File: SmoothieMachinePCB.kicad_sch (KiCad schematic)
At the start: 50 parts, among them J1 Up Button, J10 Vin, J11 LCD I2C Adapter, J2 Down Button, J3 Next Ingredient Button, J4 Next Recipe Button, J5 Solenoid Valve, J6 Stepper Motor 2, J8 Stepper Motor 1, J9 LoadCell, U1 ESP32-S3-WROOM-2, U2 FSA2567MPX, U3 DRV8825PWP, U4 VN10KN3-G, U6 NAU7802SGI, U7 XL1509-3.3

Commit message: Integrated Microcontroller Essential Stuff into Schematic and Assigned Footprints
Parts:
- added C4: 1uF, Capacitor_SMD:C_0805_2012Metric_Pad1.18x1.45mm_HandSolder, symbol Device:C
- added J12: Conn_ARM_JTAG_SWD_10, Connector_IDC:IDC-Header_2x05_P2.54mm_Vertical, symbol Connector:Conn_ARM_JTAG_SWD_10
- added J7: Conn_01x05, Connector_Molex:Molex_KK-254_AE-6410-05A_1x05_P2.54mm_Vertical, symbol Connector_Generic:Conn_01x05
- added JP1: SolderJumper_3_Open, Jumper:SolderJumper-3_P2.0mm_Open_TrianglePad1.0x1.5mm, symbol Jumper:SolderJumper_3_Open
- added JP2, JP3: SolderJumper_2_Open, Jumper:SolderJumper-2_P1.3mm_Open_TrianglePad1.0x1.5mm, symbol Jumper:SolderJumper_2_Open
- added Q1, Q2: SS8050, Package_TO_SOT_SMD:SOT-23, symbol Transistor_BJT:SS8050
- added R15, R16, R17, R7: 10k, Resistor_SMD:R_0805_2012Metric_Pad1.20x1.40mm_HandSolder, symbol Device:R
- added R2, R4: 1k, Resistor_SMD:R_0805_2012Metric_Pad1.20x1.40mm_HandSolder, symbol Device:R
- added R6: 100k, Resistor_SMD:R_0805_2012Metric_Pad1.20x1.40mm_HandSolder, symbol Device:R
- added SW1, SW2: SW_Push, Button_Switch_SMD:SW_SPST_B3S-1000, symbol Switch:SW_Push
- C6: value 22uF -> 100nF
- C7: value 0.1uF -> 10uF
- R5: value 10k -> 100k
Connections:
- net GND: now also C5.2, C4.2, J12.3 (GND), J12.5 (GND), J12.9 (GNDDetect), J7.5 (Pin_5), JP1.3 (B), SW1.1, SW2.1; no longer C5.1
- net MODE0: now also U1.7 (IO7); no longer U1.15 (IO3)
- net NSLEEP: now also U1.6 (IO6); no longer U1.16 (IO46)
- net VDD33: now also JP1.1 (A), JP2.2 (B), JP3.2 (B), R2.2, R6.1; no longer C1.1, L1.2, U7.3 (FB)
- net GPIO0_STRAPPING: now reaches U1.27 (IO0)
- net GPIO0_STRAPPING: now also C5.1, R5.2, R15.2, SW2.2
- new net: Q2.1 (B), R17.2
- new net: Q2.3 (C), R15.1
- new net: C1.1, JP2.1 (A), L1.2, U7.3 (FB)
- new net: JP1.2 (C), R4.2
- new net: Q1.3 (C), R7.1
- new net: J12.1 (VTref), JP3.1 (A)
- new net: Q1.1 (B), R16.2
- new net CHIP_PU: C4.1, J12.10 (~{RESET}), R6.2, R7.2, SW1.2, U1.3 (EN)
- new net DTR: J7.2 (Pin_2), Q2.2 (E), R16.1
- new net GPIO3_STRAPPING: R4.1, U1.15 (IO3)
- new net GPIO46_STRAPPING: R2.1, U1.16 (IO46)
- new net MTCK: J12.4 (SWCLK/TCK)
- new net MTDI: J12.8 (NC/TDI)
- new net MTDO: J12.6 (SWO/TDO)
- new net MTMS: J12.2 (SWDIO/TMS)
- new net RTS: J7.1 (Pin_1), Q1.2 (E), R17.1
- new net RX: J7.4 (Pin_4)
- new net TX: J7.3 (Pin_3)
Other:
- note added: "ESP32-S3 Essentials"

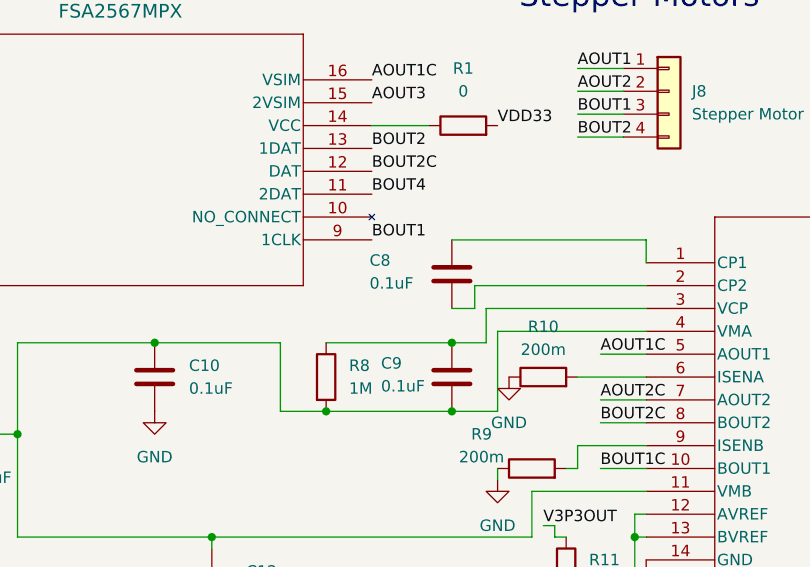
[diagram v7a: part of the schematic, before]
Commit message: Changed resistor from 0.1 to 0.01 uF in DRV8825PWP top left
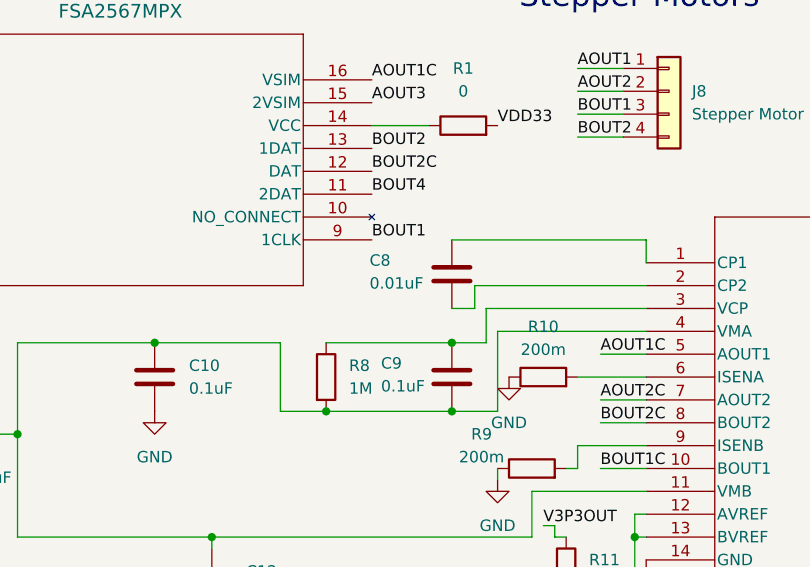
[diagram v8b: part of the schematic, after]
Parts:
- C8: value 0.1uF -> 0.01uF
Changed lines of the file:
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@@
 			)
 		)
-		(property "Value" "0.1uF"
+		(property "Value" "0.01uF"
 			(at 13.716 145.796 0)
 			(effects
